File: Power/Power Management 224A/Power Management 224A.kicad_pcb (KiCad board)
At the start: 2 copper layers, 6 parts, among them J1 USB_C_Receptacle_USB2.0_16P, Q1 2N7002, U1 AMS1117-3.3

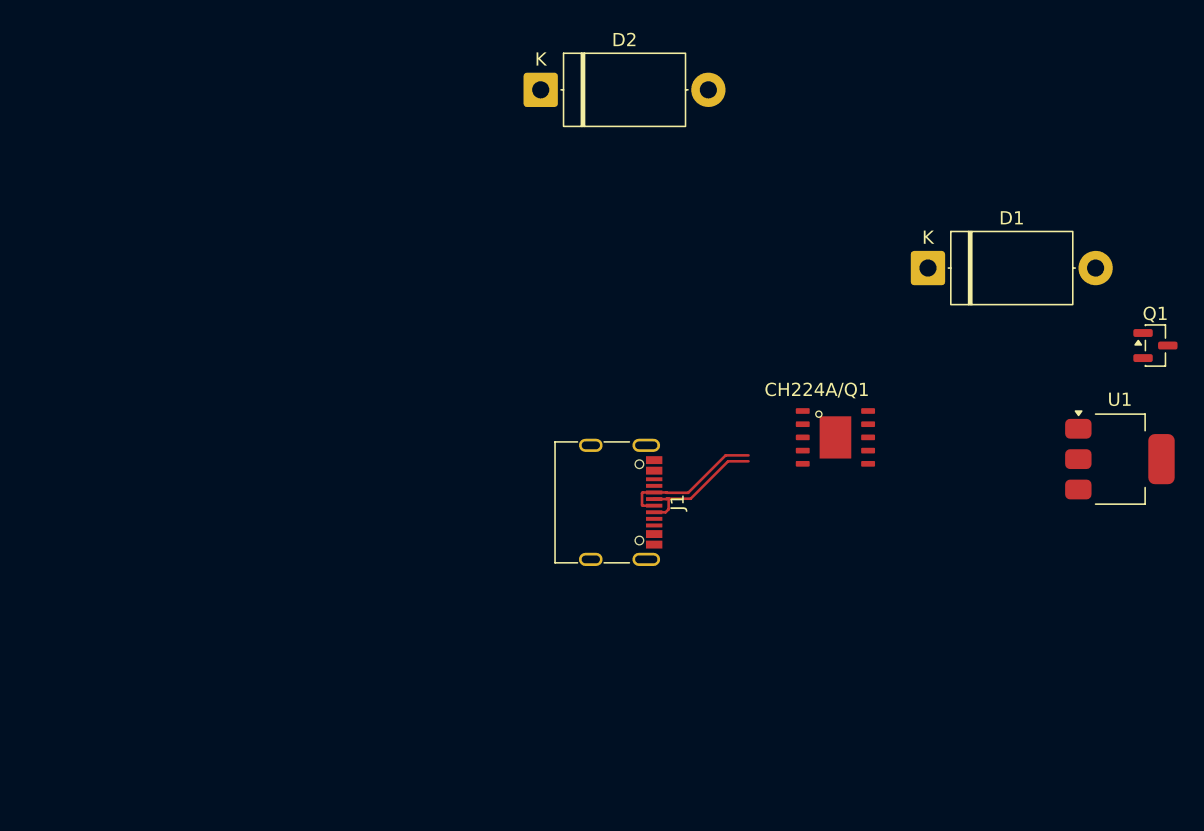
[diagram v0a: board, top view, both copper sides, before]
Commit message: New USB-Power 5V-28V
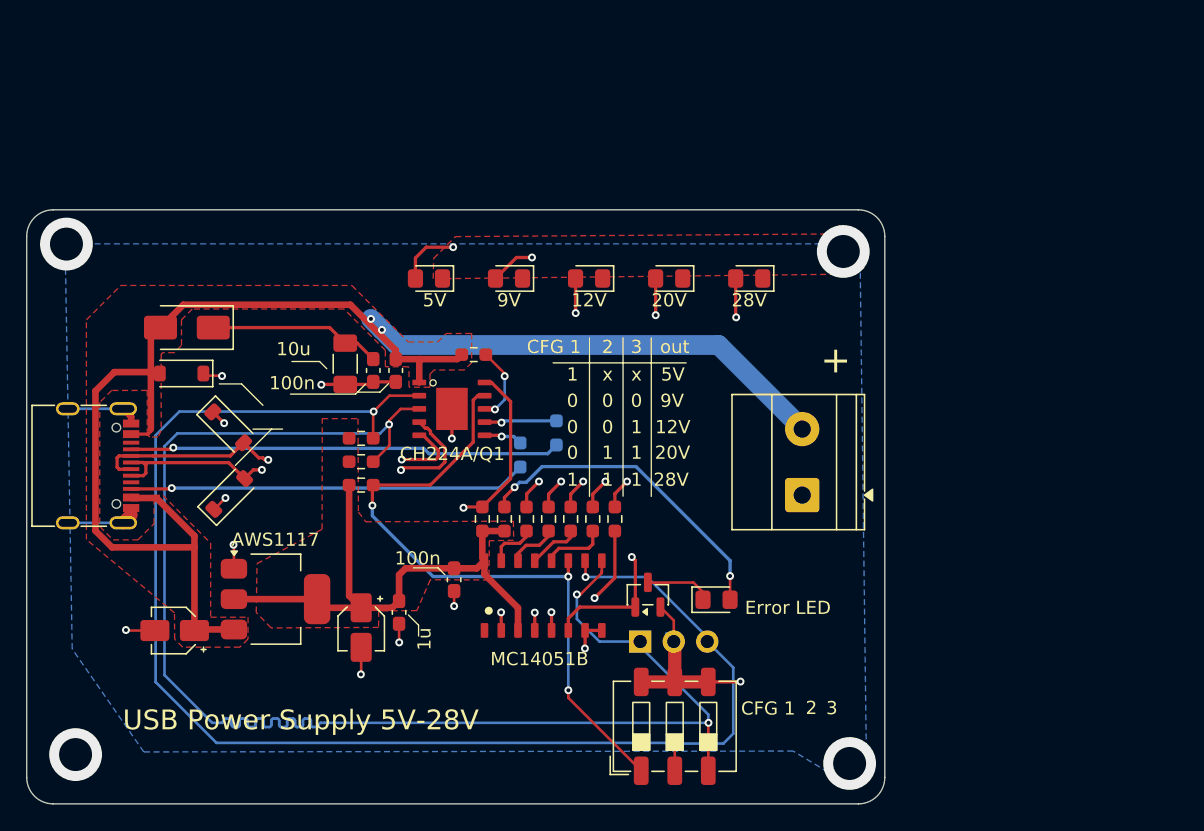
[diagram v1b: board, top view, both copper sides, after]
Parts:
- removed D1: SMAJ5.0CA, Diode_THT:D_DO-201AE_P12.70mm_Horizontal
- added +: Screw_Terminal_01x02, TerminalBlock_Phoenix:TerminalBlock_Phoenix_MKDS-1,5-2_1x02_P5.00mm_Horizontal, F.Cu at (116.8, 97.8)
- added 100k: 100k, Resistor_SMD:R_0603_1608Metric_Pad0.98x0.95mm_HandSolder, F.Cu at (91.9, 87.1)
- added 100n: 100n, Capacitor_SMD:C_0603_1608Metric_Pad1.08x0.95mm_HandSolder, F.Cu at (90.4, 104.2)
- added 100n: 10u, Capacitor_SMD:C_1206_3216Metric_Pad1.33x1.80mm_HandSolder, F.Cu at (82.2, 87.8)
- added 10k: 10k, Resistor_SMD:R_0603_1608Metric_Pad0.98x0.95mm_HandSolder, F.Cu at (92.6, 99.6)
- added 10k: 10k, Resistor_SMD:R_0603_1608Metric_Pad0.98x0.95mm_HandSolder, F.Cu at (83.4, 93.5)
- added 12V: LED, LED_SMD:LED_0805_2012Metric_Pad1.15x1.40mm_HandSolder, F.Cu at (100.7, 81.4)
- added 1K: 1k, Resistor_SMD:R_0603_1608Metric_Pad0.98x0.95mm_HandSolder, F.Cu at (102.6, 99.6)
- added 1u: 1u, Capacitor_SMD:C_0603_1608Metric_Pad1.08x0.95mm_HandSolder, F.Cu at (86.3, 106.7)
- added 20V: LED, LED_SMD:LED_0805_2012Metric_Pad1.15x1.40mm_HandSolder, F.Cu at (106.7, 81.4)
- added 28V: LED, LED_SMD:LED_0805_2012Metric_Pad1.15x1.40mm_HandSolder, F.Cu at (112.8, 81.4)
- added 5V: LED, LED_SMD:LED_0805_2012Metric_Pad1.15x1.40mm_HandSolder, F.Cu at (88.5, 81.4)
- added 9V: LED, LED_SMD:LED_0805_2012Metric_Pad1.15x1.40mm_HandSolder, F.Cu at (94.6, 81.4)
- added C2: 100n, Capacitor_SMD:C_0603_1608Metric_Pad1.08x0.95mm_HandSolder, F.Cu at (84.3, 88.3)
- added C3: 100n, Capacitor_SMD:C_0603_1608Metric_Pad1.08x0.95mm_HandSolder, F.Cu at (86.0, 88.3)
- added C5: 10u, Capacitor_SMD:CP_Elec_3x5.4, F.Cu at (69.3, 108.0)
- added C6: 10u, Capacitor_SMD:CP_Elec_3x5.4, F.Cu at (83.4, 107.8)
- added CFG 1: SW_DIP_x03, Button_Switch_SMD:SW_DIP_SPSTx03_Slide_6.7x9.18mm_W6.73mm_P2.54mm_LowProfile_JPin, F.Cu at (107.2, 115.3)
- added D3: LED, LED_SMD:LED_0805_2012Metric_Pad1.15x1.40mm_HandSolder, F.Cu at (110.3, 105.7)
- added D5: SMAJ5.0CA, Diode_SMD:D_SOD-123, F.Cu at (73.4, 97.7)
- added J2: Conn_01x03, Connector_PinHeader_2.54mm:PinHeader_1x03_P2.54mm_Vertical, B.Cu at (104.5, 108.9)
- added MC14051B: ~, Package_SOIC:SOIC-MC1405B, F.Cu at (97.2, 105.4)
- added R10: 1k, Resistor_SMD:R_0603_1608Metric_Pad0.98x0.95mm_HandSolder, F.Cu at (97.6, 99.6)
- added R11: 1k, Resistor_SMD:R_0603_1608Metric_Pad0.98x0.95mm_HandSolder, F.Cu at (99.3, 99.6)
- added R13: 1k, Resistor_SMD:R_0603_1608Metric_Pad0.98x0.95mm_HandSolder, F.Cu at (94.3, 99.6)
- added R3: 10k, Resistor_SMD:R_0603_1608Metric_Pad0.98x0.95mm_HandSolder, F.Cu at (83.4, 97.0)
- added R4: 10k, Resistor_SMD:R_0603_1608Metric_Pad0.98x0.95mm_HandSolder, F.Cu at (83.4, 95.2)
- added R6: 10, Resistor_SMD:R_0603_1608Metric_Pad0.98x0.95mm_HandSolder, B.Cu at (98.2, 93.1)
- added R7: 10, Resistor_SMD:R_0603_1608Metric_Pad0.98x0.95mm_HandSolder, B.Cu at (95.5, 94.7)
- added R8: 1k, Resistor_SMD:R_0603_1608Metric_Pad0.98x0.95mm_HandSolder, F.Cu at (100.9, 99.6)
- added R9: 1k, Resistor_SMD:R_0603_1608Metric_Pad0.98x0.95mm_HandSolder, F.Cu at (95.9, 99.6)
- added SMAJ: SMAJ5.0CA, Diode_SMD:D_SOD-123, F.Cu at (73.3, 92.6)
- added SS34: SS34, Diode_SMD:D_SMA, F.Cu at (70.2, 85.1)
- D2: footprint Diode_THT:D_DO-201AE_P12.70mm_Horizontal -> Diode_SMD:D_SOD-123
- moved AWS1117 64.8 mm to (76.9, 105.7)
- moved 2N7002 42.8 mm to (105.1, 105.3), turned to 90 degrees
- moved J1 39.7 mm to (62.2, 95.6)
- moved D2 34.7 mm to (69.8, 88.6), turned to 180 degrees
- moved CH224A/Q1 29.1 mm to (90.3, 91.2)
- renumbered Q1 to 2N7002, U1 to AWS1117
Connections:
- AWS1117 pad 3: VBUS -> V_USB
- CH224A/Q1 pad 1: VBUS -> V_USB
- CH224A/Q1 pad 6: (no net) -> /CC2
- CH224A/Q1 pad 8: /CC2 -> Net-(CH224A/Q1-VBUS)
- D2 pad 2: /USB_N -> V_USB
- J1 pad A4: VBUS -> V_USB
- J1 pad A5: /CC1 -> Net-(J1-CC1)
- J1 pad A9: VBUS -> V_USB
- J1 pad B4: VBUS -> V_USB
- J1 pad B5: /CC2 -> Net-(J1-CC2)
- J1 pad B9: VBUS -> V_USB
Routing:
- net V_USB: track 0.00 -> 113.1 mm, vias 0 -> 2
- net /CFG3/ SDA: track 0.00 -> 112.5 mm, vias 0 -> 3
- net /CGF2/ SCL: track 0.00 -> 110.6 mm, vias 0 -> 3
- net /CFG1: track 0.00 -> 50.5 mm, vias 0 -> 3
- net GND: track 0.00 -> 48.6 mm, vias 0 -> 15
- net +3.3V: track 0.00 -> 41.7 mm
- net Net-(D6-A): track 0.00 -> 37.8 mm, vias 0 -> 2
- net /PG: track 0.00 -> 37.8 mm, vias 0 -> 2
- net Net-(D7-A): track 0.00 -> 37.2 mm, vias 0 -> 2
- net Net-(J1-CC1): track 0.00 -> 32.8 mm, vias 0 -> 1
- net Net-(J1-CC2): track 0.00 -> 30.2 mm, vias 0 -> 1
- net /USB_P: track 10.3 -> 35.1 mm, vias 0 -> 2
- net Net-(D3-A): track 0.00 -> 24.7 mm, vias 0 -> 2
- net /USB_N: track 11.1 -> 34.2 mm, vias 0 -> 2
- net Net-(D10-A): track 0.00 -> 22.2 mm, vias 0 -> 2
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- added copper zone on F.Cu, net +3.3V
- added copper zone on B.Cu, net GND
- added copper zone on F.Cu, net GND
- added copper zone on In1.Cu, net GND
- added copper zone on In2.Cu, net GND
- added copper zone on F.Cu, net V_USB
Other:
- board outline added: 65 x 45 mm
- copper layers 2 -> 4
- board text added: "0"
- board text added: "1"
- board text added: "10u"
- board text added: "12V"
- board text added: "2"
- board text added: "20V"
- board text added: "28V"
- board text added: "3"
- board text added: "5V"
- board text added: "9V"
- board text added: "CFG 1"
- board text added: "Error LED"
- board text added: "GND"
- board text added: "SCL"
- board text added: "USB Power Supply 5V-28V"
- board text added: "out"
- board text added: "x"

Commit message: Update Viapad
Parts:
- removed the 100n at (82.2, 87.8)
- added C1: 10u, Capacitor_SMD:C_1206_3216Metric_Pad1.33x1.80mm_HandSolder, F.Cu at (82.0, 87.5)
- added C8: 100n, Capacitor_SMD:C_0603_1608Metric_Pad1.08x0.95mm_HandSolder, F.Cu at (94.4, 109.9)
- CFG1: renamed from CFG 1
- moved SS34 0.88 mm to (71.1, 85.1)
- moved 100n 0.86 mm to (90.7, 103.4)
- moved C3 0.48 mm to (86.2, 87.9)
- moved C2 0.42 mm to (84.3, 87.9)
- renumbered J2 to SDA
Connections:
- C2 pad 1: Net-(D1-K) -> V_USB
- D2 pad 2: V_USB -> Net-(D1-K)
- J1 pad A4: V_USB -> Net-(D1-K)
- J1 pad A9: V_USB -> Net-(D1-K)
- J1 pad B4: V_USB -> Net-(D1-K)
- J1 pad B9: V_USB -> Net-(D1-K)
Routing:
- net V_USB: track 113.1 -> 104.5 mm
- net Net-(D1-K): track 13.1 -> 19.5 mm
- net /CFG3/ SDA: track 112.5 -> 108.9 mm
- net GND: track 48.6 -> 51.1 mm, vias 15 -> 87
- net /USB_N: track 34.2 -> 32.8 mm
- net (no net): vias 1 -> 0
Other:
- board text added: "100n"
